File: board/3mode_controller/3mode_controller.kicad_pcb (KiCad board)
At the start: 2 copper layers, 110 x 50 mm, 48 parts, among them IC1 DW01A, J1 Conn_01x04_Socket, J2 USB_C_Receptacle, Q1 FDN336P, SW1 reset, SW2 boot, SW3 ChangeScreen, SW4 SW_SPDT, U1 TP4056, U2 ESP32-S3-WROOM-1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

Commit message: first prototype board
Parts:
- removed C6: 10u, Capacitor_SMD:C_0603_1608Metric_Pad1.08x0.95mm_HandSolder
- removed H3, H4: MountingHole, MountingHole:MountingHole_3.2mm_M3_ISO14580_Pad
- removed U3: 18350-HOLDER, CustomFootprints:18350-Holder
- removed kibuzzard-662557F7: G***, kibuzzard-662557F7
- removed kibuzzard-66255824: G***, kibuzzard-66255824
- removed kibuzzard-6625583C: G***, kibuzzard-6625583C
- removed kibuzzard-662558AB: G***, kibuzzard-662558AB
- C1, C3, C5, R1, U2: moved to F.Cu
- J1: value Conn_01x04_Socket -> JST XH; footprint Connector_PinHeader_2.54mm:PinHeader_1x04_P2.54mm_Vertical -> Connector_JST:JST_PH_S2B-PH-K_1x02_P2.00mm_Horizontal
- SW3: value ChangeScreen -> SW_DIP_x04; footprint Button_Switch_THT:SW_PUSH_6mm -> Button_Switch_THT:SW_DIP_SPSTx04_Slide_9.78x12.34mm_W7.62mm_P2.54mm
- moved kibuzzard-662557D5 232.6 mm to (346.0, 147.5), turned to -90 degrees
- moved kibuzzard-66255BA9 227.2 mm to (343.1, 150.0), turned to -90 degrees
- moved kibuzzard-66255856 222.6 mm to (340.5, 151.5), turned to -90 degrees
- moved SW2 187.5 mm to (313.0, 135.5), turned to 0 degrees
- moved C1 186.6 mm to (299.5, 152.0), turned to -90 degrees
- moved SW1 185.6 mm to (302.5, 155.2)
- moved U6 177.9 mm to (312.6, 128.9)
- moved H1 174.9 mm to (275.5, 126.0)
- moved J1 174.7 mm to (332.0, 126.0), turned to 180 degrees
- moved R3 165.9 mm to (317.1, 158.6), turned to 90 degrees
- moved R4 165.9 mm to (318.9, 158.6), turned to -90 degrees
- moved C5 163.3 mm to (283.2, 130.8)
- moved R1 162.2 mm to (283.2, 129.0), turned to 0 degrees
- moved C3 162.1 mm to (283.2, 127.2)
- moved D1 160.7 mm to (320.6, 158.5)
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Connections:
- J1 pad 1: GND -> VBAT+PROTECT
- J1 pad 2: +3.3V -> Net-(IC1-GND)
- SW3 pad 1: ESP32_BUTTON -> ESP32-PULLUP-4
- SW3 pad 2: GND -> ESP32-PULLUP-3
- U2 pad 10: unconnected-(U2-GPIO17/U1TXD/ADC2_CH6-Pad10) -> JS_RIGHT_IRQ
- U2 pad 12: ESP32_SCREEN_SCK -> ESP32-PULLUP-3
- U2 pad 17: ESP32_SCREEN_SDA -> ESP32-PULLUP-4
- U2 pad 22: unconnected-(U2-GPIO14/TOUCH14/ADC2_CH3/FSPIWP/FSPIDQS/SUBSPIWP-Pad22) -> JS_LEFT_IRQ
- U2 pad 5: ESP32_BUTTON -> unconnected-(U2-GPIO5/TOUCH5/ADC1_CH4-Pad5)
- U2 pad 6: unconnected-(U2-GPIO6/TOUCH6/ADC1_CH5-Pad6) -> ESP32-PULLUP-1
- U2 pad 7: unconnected-(U2-GPIO7/TOUCH7/ADC1_CH6-Pad7) -> ESP32-PULLUP-2
- U7 pad 7: unconnected-(U7-SWa-Pad7) -> GND
- U7 pad 8: unconnected-(U7-SWb-Pad8) -> JS_LEFT_IRQ
- U7 pad 9: GND -> unconnected-(U7-SWc-Pad9)
- U8 pad 7: unconnected-(U8-SWa-Pad7) -> GND
- U8 pad 8: unconnected-(U8-SWb-Pad8) -> JS_RIGHT_IRQ
- U8 pad 9: GND -> unconnected-(U8-SWc-Pad9)
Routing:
- net JS_RIGHT_IRQ: track 0.00 -> 86.2 mm, vias 0 -> 1
- net ESP32_BUTTON: track 79.1 -> 0.00 mm, vias 2 -> 0
- net Net-(IC1-GND): track 99.5 -> 26.4 mm, vias 1 -> 0
- net JS_LEFT_IRQ: track 0.00 -> 46.3 mm, vias 0 -> 1
- net ESP32_JOYSTICK_Y: track 34.4 -> 60.7 mm
- net ESP32_SCREEN_SDA: track 21.2 -> 0.00 mm
- net ESP32_RF_SPI_CE: track 51.7 -> 31.6 mm
- net ESP32_RF_SPI_MISO: track 51.4 -> 31.6 mm, vias 0 -> 1
- net ESP32_SCREEN_SCK: track 19.1 -> 0.00 mm
- net VBAT+PROTECT: track 29.0 -> 46.3 mm
- net ESP32_RF_SPI_SCK: track 48.0 -> 31.3 mm, vias 0 -> 1
- net ESP32-BOOT0: track 26.6 -> 10.9 mm, vias 1 -> 0
- net +5V: track 50.2 -> 35.9 mm
- net ESP32_RF_SPI_CNS: track 46.3 -> 32.7 mm
- net +3.3V: track 175.8 -> 189.3 mm, vias 4 -> 1
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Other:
- board size 110 x 50 mm -> 100 x 71 mm
- board text added: "+"

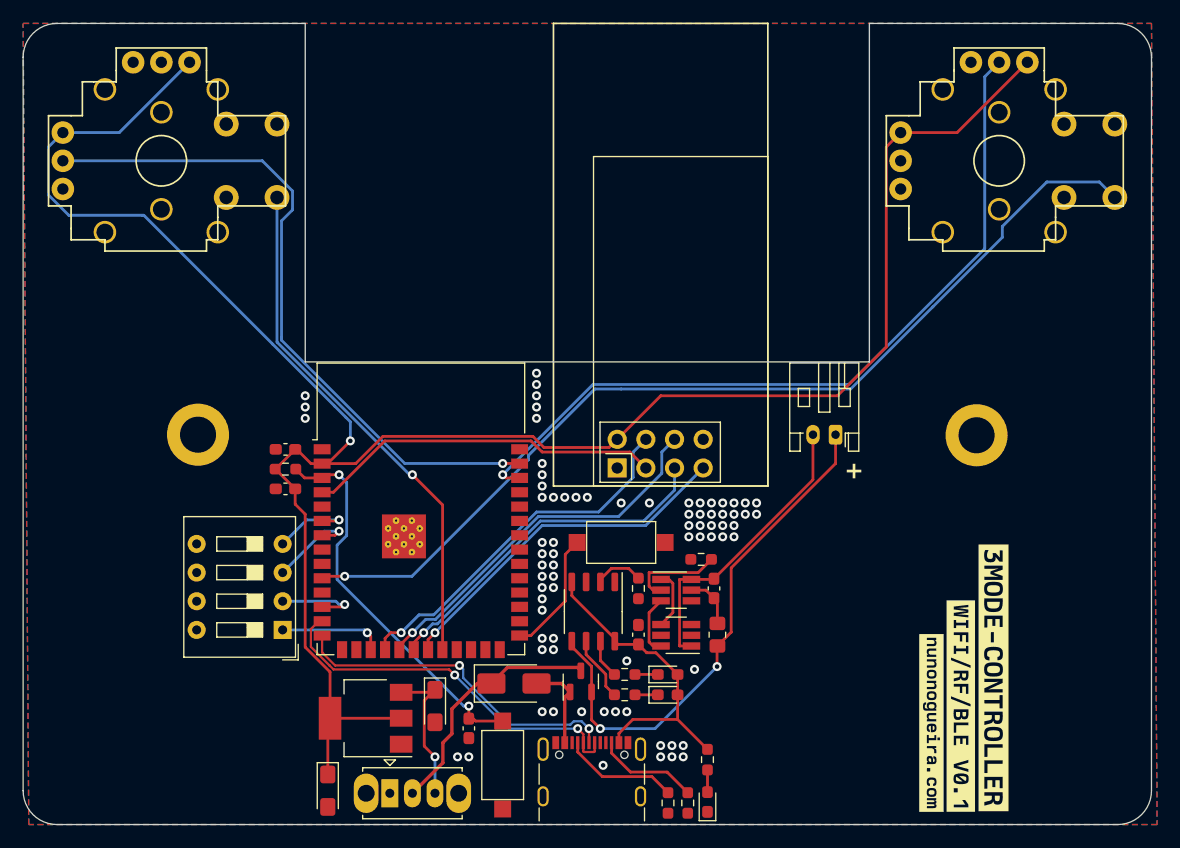
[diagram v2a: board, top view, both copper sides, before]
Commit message: v0.2.
Replaced diode and LDO
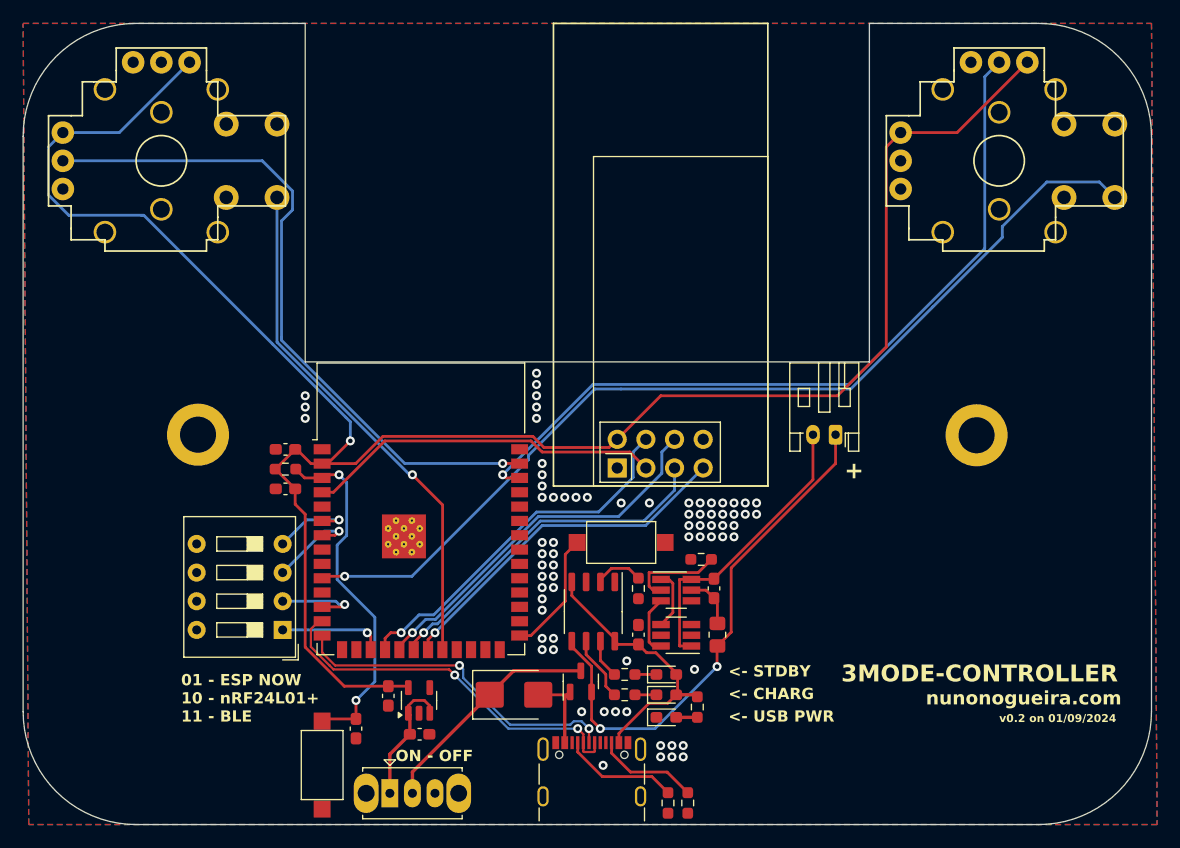
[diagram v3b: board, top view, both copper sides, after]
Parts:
- removed C7, C8: 10u, Capacitor_Tantalum_SMD:CP_EIA-3216-18_Kemet-A_Pad1.58x1.35mm_HandSolder
- removed U5: AMS1117-3.3, Package_TO_SOT_SMD:SOT-223-3_TabPin2
- removed kibuzzard-662557D5: G***, kibuzzard-662557D5
- removed kibuzzard-66255856: G***, kibuzzard-66255856
- removed kibuzzard-66255BA9: G***, kibuzzard-66255BA9
- added C6: 1u, Capacitor_SMD:C_0603_1608Metric_Pad1.08x0.95mm_HandSolder, F.Cu at (295.1, 152.5)
- added C9: 1u, Capacitor_SMD:C_0603_1608Metric_Pad1.08x0.95mm_HandSolder, F.Cu at (292.4, 149.1)
- added U3: AP2112K-3.3, Package_TO_SOT_SMD:SOT-23-5, F.Cu at (295.1, 149.5)
- D4: value SS14 -> VS-10BQ015HM3/5BT; footprint Diode_SMD:D_SMA -> Diode_SMD:D_SMB
- moved SW1 16.0 mm to (286.5, 155.2)
- moved C1 10.0 mm to (289.5, 152.0)
- moved D1 8.34 mm to (317.0, 151.0), turned to 0 degrees
- moved R7 4.75 mm to (319.8, 150.1)
- moved D4 1.00 mm to (303.5, 149.0)
- moved D2 0.12 mm to (317.0, 147.2)
- moved D3 0.12 mm to (317.0, 149.0)
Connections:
- SW4 pad 1: unconnected-(SW4-A-Pad1) -> Net-(SW4-A)
- SW4 pad 3: Net-(SW4-C) -> unconnected-(SW4-C-Pad3)
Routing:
- net Net-(SW4-C): track 13.3 -> 0.00 mm, vias 1 -> 0
- net Net-(SW4-A): track 0.00 -> 11.5 mm
- net +3.3V: track 189.3 -> 181.3 mm
- net +5V: track 35.9 -> 32.3 mm
- net ESP32-RESET: track 34.7 -> 31.7 mm
- net VSPLY: track 22.0 -> 20.5 mm
- net GND: vias 75 -> 71
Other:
- outline, holes or cut-outs redrawn
- board text added: "01 - ESP NOW 10 - nRF24L01+ 11 - BLE"
- board text added: "3MODE-CONTROLLER"
- board text added: "<- CHARG"
- board text added: "<- STDBY"
- board text added: "<- USB PWR"
- board text added: "ON - OFF"
- board text added: "nunonogueira.com"
- board text added: "v0.2 on 01/09/2024"
